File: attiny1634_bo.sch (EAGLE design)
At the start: 11 parts, among them J1 AVR_SPI_PRG_6NS, Y1 12MHz

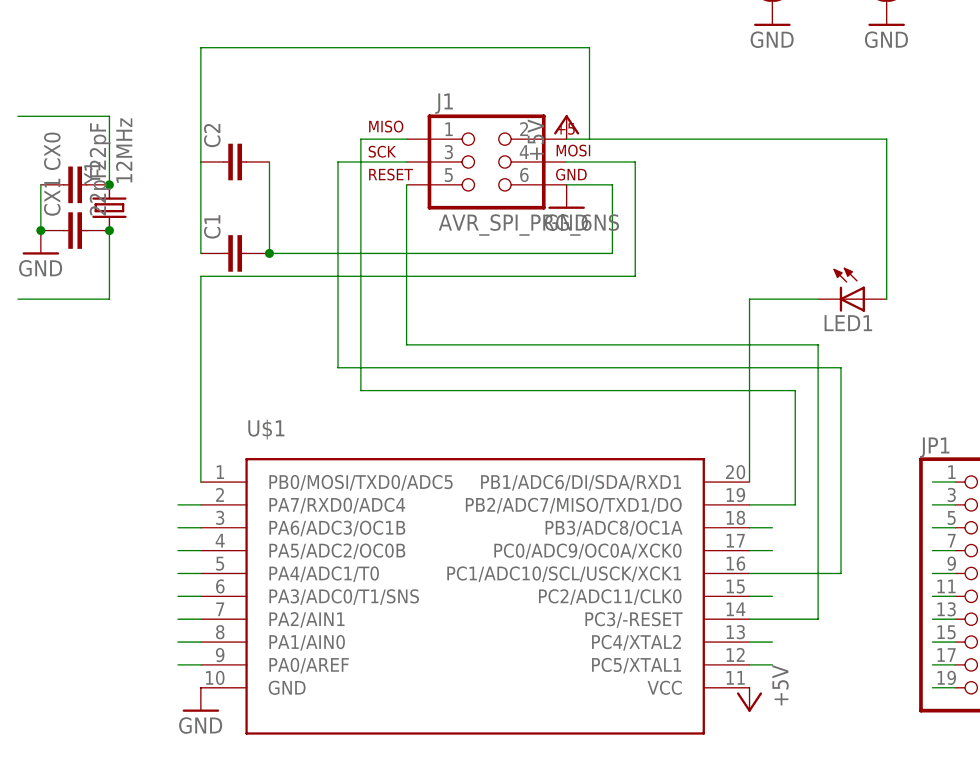
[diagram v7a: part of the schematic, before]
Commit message: shite, the MOSI is was marked to wrong pin...
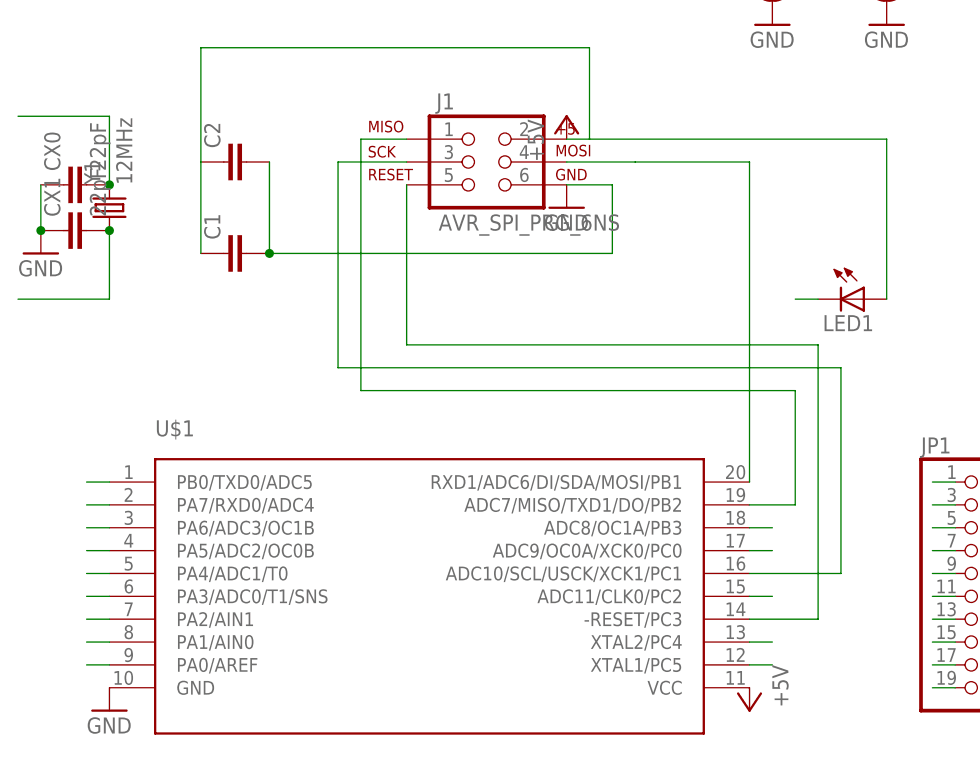
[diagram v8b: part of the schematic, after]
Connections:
- removed net PB0/MOSI/TX0/ADC5: J1.4, JP1.16, U$1.PB0/MOSI/TXD0/ADC5
- new net PB0/TXD0: U$1.PB0/TXD0/ADC5
- new net PB1/MOSI/ADC6: J1.4, JP1.16, U$1.RXD1/ADC6/DI/SDA/MOSI/PB1
- net PA0: no longer U$1.PA0/AREF
- net PA1: no longer U$1.PA1/AIN0
- net PA2: no longer U$1.PA2/AIN1
- net PA3: no longer U$1.PA3/ADC0/T1/SNS
- net PA4: no longer U$1.PA4/ADC1/T0
- net PA5: no longer U$1.PA5/ADC2/OC0B
- net PA6: no longer U$1.PA6/ADC3/OC1B
- net PA7: no longer U$1.PA7/RXD0/ADC4
- net PB1/ADC6/RX1: no longer LED1.C, U$1.PB1/ADC6/DI/SDA/RXD1
- net PB2/ADC7/TX1: now also U$1.ADC7/MISO/TXD1/DO/PB2; no longer U$1.PB2/ADC7/MISO/TXD1/DO
- net PB3/ADC8/OC1A: now also U$1.ADC8/OC1A/PB3; no longer U$1.PB3/ADC8/OC1A
- net PC0/ADC9/OC0A: now also LED1.C, U$1.ADC9/OC0A/XCK0/PC0; no longer U$1.PC0/ADC9/OC0A/XCK0
- net PC1/SCL/ADC10: now also U$1.ADC10/SCL/USCK/XCK1/PC1; no longer U$1.PC1/ADC10/SCL/USCK/XCK1
- net PC2/ADC11: now also U$1.ADC11/CLK0/PC2; no longer U$1.PC2/ADC11/CLK0
- net PC3/-RESET: now also U$1.-RESET/PC3; no longer U$1.PC3/-RESET
- net PC4/XTAL2: now also U$1.XTAL2/PC4; no longer U$1.PC4/XTAL2
- net PC5/XTAL1: now also U$1.XTAL1/PC5; no longer U$1.PC5/XTAL1
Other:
- moved on the sheet: U$1
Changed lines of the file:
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@@
 <part name="P+3" library="supply1" deviceset="+5V" device=""/>
 <part name="GND2" library="supply1" deviceset="GND" device=""/>
-<part name="U$1" library="attiny1634" deviceset="ATTINY1634" device=""/>
 <part name="P+1" library="supply1" deviceset="+5V" device=""/>
 <part name="GND1" library="supply1" deviceset="GND" device=""/>
+<part name="U$1" library="attiny1634" deviceset="ATTINY1634" device=""/>
 </parts>
 <sheets>
@@
 <instance part="P+3" gate="1" x="127" y="45.72" rot="R180"/>
 <instance part="GND2" gate="1" x="129.54" y="50.8" rot="R90"/>
-<instance part="U$1" gate="G$1" x="66.04" y="71.12"/>
 <instance part="P+1" gate="1" x="96.52" y="45.72" rot="R180"/>
-<instance part="GND1" gate="1" x="35.56" y="45.72"/>
+<instance part="GND1" gate="1" x="25.4" y="45.72"/>
+<instance part="U$1" gate="G$1" x="55.88" y="71.12"/>
 </instances>
 <busses>
@@
 </segment>
 <segment>
+<pinref part="P+1" gate="1" pin="+5V"/>
 <pinref part="U$1" gate="G$1" pin="VCC"/>
-<pinref part="P+1" gate="1" pin="+5V"/>
 </segment>
 </net>
 <net name="PB1/ADC6/RX1" class="0">
-<segment>
-<pinref part="LED1" gate="G$1" pin="C"/>
-<wire x1="96.52" y1="91.44" x2="104.14" y2="91.44" width="0.1524" layer="91"/>
-<pinref part="U$1" gate="G$1" pin="PB1/ADC6/DI/SDA/RXD1"/>
-<wire x1="96.52" y1="71.12" x2="96.52" y2="91.44" width="0.1524" layer="91"/>
-</segment>
 <segment>
 <pinref part="JP1" gate="A" pin="14"/>
@@
 </segment>
 </net>
-<net name="PB0/MOSI/TX0/ADC5" class="0">
-<segment>
-<pinref part="J1" gate="G$1" pin="4"/>
-<wire x1="76.2" y1="106.68" x2="83.82" y2="106.68" width="0.1524" layer="91"/>
-<wire x1="83.82" y1="106.68" x2="83.82" y2="93.98" width="0.1524" layer="91"/>
-<pinref part="U$1" gate="G$1" pin="PB0/MOSI/TXD0/ADC5"/>
-<wire x1="83.82" y1="93.98" x2="35.56" y2="93.98" width="0.1524" layer="91"/>
-<wire x1="35.56" y1="93.98" x2="35.56" y2="71.12" width="0.1524" layer="91"/>
-</segment>
-<segment>
-<pinref part="JP1" gate="A" pin="16"/>
-<wire x1="127" y1="53.34" x2="129.54" y2="53.34" width="0.1524" layer="91"/>
-</segment>
-</net>
 <net name="PC1/SCL/ADC10" class="0">
 <segment>
-<pinref part="U$1" gate="G$1" pin="PC1/ADC10/SCL/USCK/XCK1"/>
 <wire x1="96.52" y1="60.96" x2="106.68" y2="60.96" width="0.1524" layer="91"/>
 <wire x1="106.68" y1="60.96" x2="106.68" y2="83.82" width="0.1524" layer="91"/>
@@
 <pinref part="J1" gate="G$1" pin="3"/>
 <wire x1="50.8" y1="106.68" x2="58.42" y2="106.68" width="0.1524" layer="91"/>
+<pinref part="U$1" gate="G$1" pin="ADC10/SCL/USCK/XCK1/PC1"/>
 </segment>
 <segment>
@@
 <net name="PB2/ADC7/TX1" class="0">
 <segment>
-<pinref part="U$1" gate="G$1" pin="PB2/ADC7/MISO/TXD1/DO"/>
 <wire x1="96.52" y1="68.58" x2="101.6" y2="68.58" width="0.1524" layer="91"/>
 <wire x1="101.6" y1="68.58" x2="101.6" y2="81.28" width="0.1524" layer="91"/>
@@
 <pinref part="J1" gate="G$1" pin="1"/>
 <wire x1="53.34" y1="109.22" x2="58.42" y2="109.22" width="0.1524" layer="91"/>
+<pinref part="U$1" gate="G$1" pin="ADC7/MISO/TXD1/DO/PB2"/>
 </segment>
 <segment>
@@
 <net name="PC3/-RESET" class="0">
 <segment>
-<pinref part="U$1" gate="G$1" pin="PC3/-RESET"/>
 <wire x1="96.52" y1="55.88" x2="104.14" y2="55.88" width="0.1524" layer="91"/>
 <wire x1="104.14" y1="55.88" x2="104.14" y2="86.36" width="0.1524" layer="91"/>
@@
 <wire x1="104.14" y1="86.36" x2="58.42" y2="86.36" width="0.1524" layer="91"/>
 <wire x1="58.42" y1="86.36" x2="58.42" y2="104.14" width="0.1524" layer="91"/>
+<pinref part="U$1" gate="G$1" pin="-RESET/PC3"/>
 </segment>
 </net>
 <net name="PC5/XTAL1" class="0">
 <segment>
-<pinref part="U$1" gate="G$1" pin="PC5/XTAL1"/>
 <wire x1="96.52" y1="50.8" x2="99.06" y2="50.8" width="0.1524" layer="91"/>
+<pinref part="U$1" gate="G$1" pin="XTAL1/PC5"/>
 </segment>
 <segment>
@@
 <net name="PC4/XTAL2" class="0">
 <segment>
-<pinref part="U$1" gate="G$1" pin="PC4/XTAL2"/>
 <wire x1="96.52" y1="53.34" x2="99.06" y2="53.34" width="0.1524" layer="91"/>
+<pinref part="U$1" gate="G$1" pin="XTAL2/PC4"/>
 </segment>
 <segment>
@@
 <net name="PA0" class="0">
 <segment>
-<pinref part="U$1" gate="G$1" pin="PA0/AREF"/>
-<wire x1="35.56" y1="50.8" x2="33.02" y2="50.8" width="0.1524" layer="91"/>
+<wire x1="25.4" y1="50.8" x2="22.86" y2="50.8" width="0.1524" layer="91"/>
 </segment>
 <segment>
@@
 <net name="PA1" class="0">
 <segment>
-<pinref part="U$1" gate="G$1" pin="PA1/AIN0"/>
-<wire x1="35.56" y1="53.34" x2="33.02" y2="53.34" width="0.1524" layer="91"/>
+<wire x1="25.4" y1="53.34" x2="22.86" y2="53.34" width="0.1524" layer="91"/>
 </segment>
 <segment>
@@
 </segment>
 <segment>
-<pinref part="U$1" gate="G$1" pin="PA5/ADC2/OC0B"/>
-<wire x1="35.56" y1="63.5" x2="33.02" y2="63.5" width="0.1524" layer="91"/>
+<wire x1="25.4" y1="63.5" x2="22.86" y2="63.5" width="0.1524" layer="91"/>
 </segment>
 </net>
@@
 </segment>
 <segment>
-<pinref part="U$1" gate="G$1" pin="PA4/ADC1/T0"/>
-<wire x1="35.56" y1="60.96" x2="33.02" y2="60.96" width="0.1524" layer="91"/>
+<wire x1="25.4" y1="60.96" x2="22.86" y2="60.96" width="0.1524" layer="91"/>
 </segment>
 </net>
@@
 </segment>
 <segment>
-<pinref part="U$1" gate="G$1" pin="PA3/ADC0/T1/SNS"/>
-<wire x1="35.56" y1="58.42" x2="33.02" y2="58.42" width="0.1524" layer="91"/>
+<wire x1="25.4" y1="58.42" x2="22.86" y2="58.42" width="0.1524" layer="91"/>
 </segment>
 </net>
@@
 </segment>
 <segment>
-<pinref part="U$1" gate="G$1" pin="PA2/AIN1"/>
-<wire x1="35.56" y1="55.88" x2="33.02" y2="55.88" width="0.1524" layer="91"/>
+<wire x1="25.4" y1="55.88" x2="22.86" y2="55.88" width="0.1524" layer="91"/>
 </segment>
 </net>
@@
 </segment>
 <segment>
-<pinref part="U$1" gate="G$1" pin="PA7/RXD0/ADC4"/>
-<wire x1="35.56" y1="68.58" x2="33.02" y2="68.58" width="0.1524" layer="91"/>
+<wire x1="25.4" y1="68.58" x2="22.86" y2="68.58" width="0.1524" layer="91"/>
 </segment>
 </net>
@@
 </segment>
 <segment>
-<pinref part="U$1" gate="G$1" pin="PA6/ADC3/OC1B"/>
-<wire x1="35.56" y1="66.04" x2="33.02" y2="66.04" width="0.1524" layer="91"/>
+<wire x1="25.4" y1="66.04" x2="22.86" y2="66.04" width="0.1524" layer="91"/>
 </segment>
 </net>
 <net name="PB3/ADC8/OC1A" class="0">
 <segment>
-<pinref part="U$1" gate="G$1" pin="PB3/ADC8/OC1A"/>
 <wire x1="96.52" y1="66.04" x2="99.06" y2="66.04" width="0.1524" layer="91"/>
+<pinref part="U$1" gate="G$1" pin="ADC8/OC1A/PB3"/>
 </segment>
 <segment>
@@
 <net name="PC0/ADC9/OC0A" class="0">
 <segment>
-<pinref part="U$1" gate="G$1" pin="PC0/ADC9/OC0A/XCK0"/>
 <wire x1="96.52" y1="63.5" x2="99.06" y2="63.5" width="0.1524" layer="91"/>
+<pinref part="U$1" gate="G$1" pin="ADC9/OC0A/XCK0/PC0"/>
 </segment>
 <segment>
@@
 <wire x1="127" y1="63.5" x2="129.54" y2="63.5" width="0.1524" layer="91"/>
 </segment>
+<segment>
+<pinref part="LED1" gate="G$1" pin="C"/>
+<wire x1="104.14" y1="91.44" x2="101.6" y2="91.44" width="0.1524" layer="91"/>
+</segment>
 </net>
 <net name="PC2/ADC11" class="0">
 <segment>
-<pinref part="U$1" gate="G$1" pin="PC2/ADC11/CLK0"/>
 <wire x1="96.52" y1="58.42" x2="99.06" y2="58.42" width="0.1524" layer="91"/>
+<pinref part="U$1" gate="G$1" pin="ADC11/CLK0/PC2"/>
 </segment>
 <segment>
@@
 </segment>
 </net>
+<net name="PB0/TXD0" class="0">
+<segment>
+<pinref part="U$1" gate="G$1" pin="PB0/TXD0/ADC5"/>
+<wire x1="25.4" y1="71.12" x2="22.86" y2="71.12" width="0.1524" layer="91"/>
+</segment>
+</net>
+<net name="PB1/MOSI/ADC6" class="0">
+<segment>
+<pinref part="J1" gate="G$1" pin="4"/>
+<wire x1="76.2" y1="106.68" x2="83.82" y2="106.68" width="0.1524" layer="91"/>
+<pinref part="U$1" gate="G$1" pin="RXD1/ADC6/DI/SDA/MOSI/PB1"/>
+<wire x1="96.52" y1="71.12" x2="96.52" y2="106.68" width="0.1524" layer="91"/>
+<wire x1="96.52" y1="106.68" x2="83.82" y2="106.68" width="0.1524" layer="91"/>
+</segment>
+<segment>
+<pinref part="JP1" gate="A" pin="16"/>
+<wire x1="127" y1="53.34" x2="129.54" y2="53.34" width="0.1524" layer="91"/>
+</segment>
+</net>
